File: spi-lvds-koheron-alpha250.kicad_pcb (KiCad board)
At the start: 2 copper layers, 55 x 50 mm, 17 parts

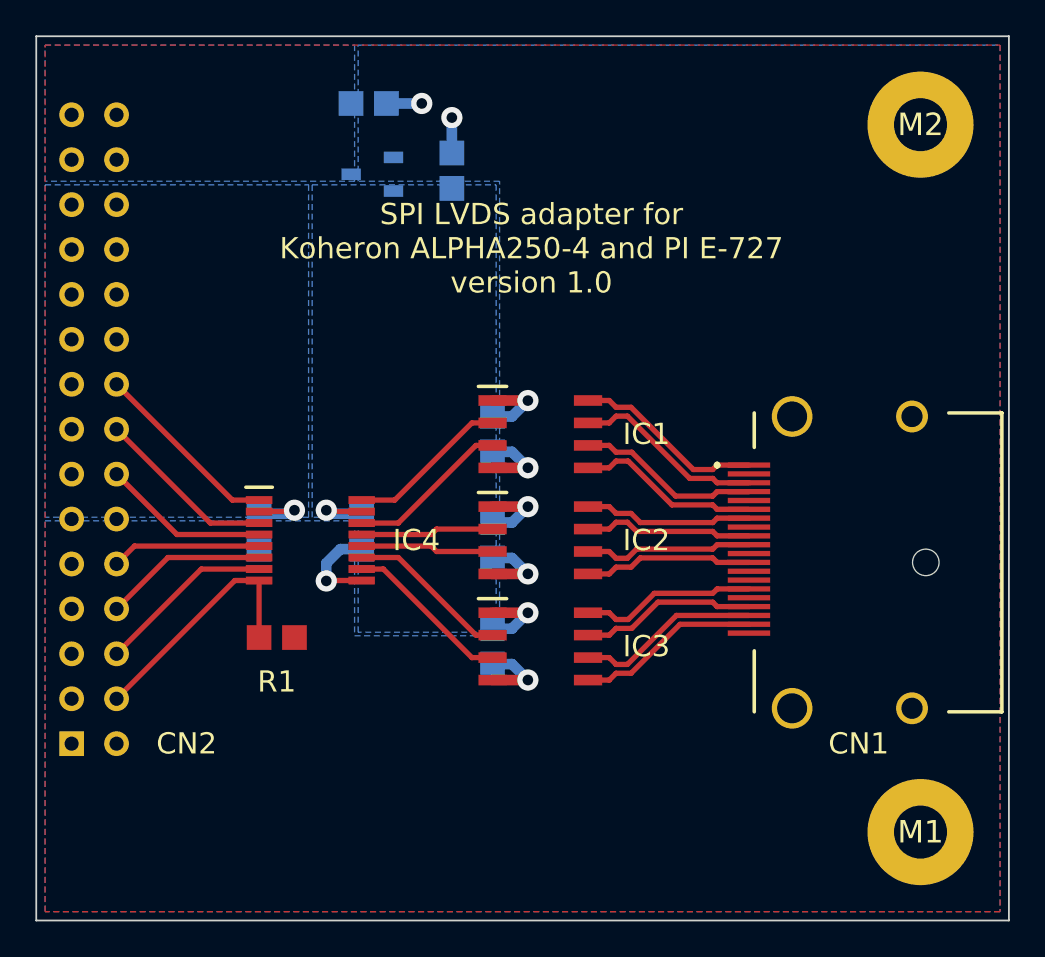
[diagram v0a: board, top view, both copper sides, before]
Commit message: improve PCB layout
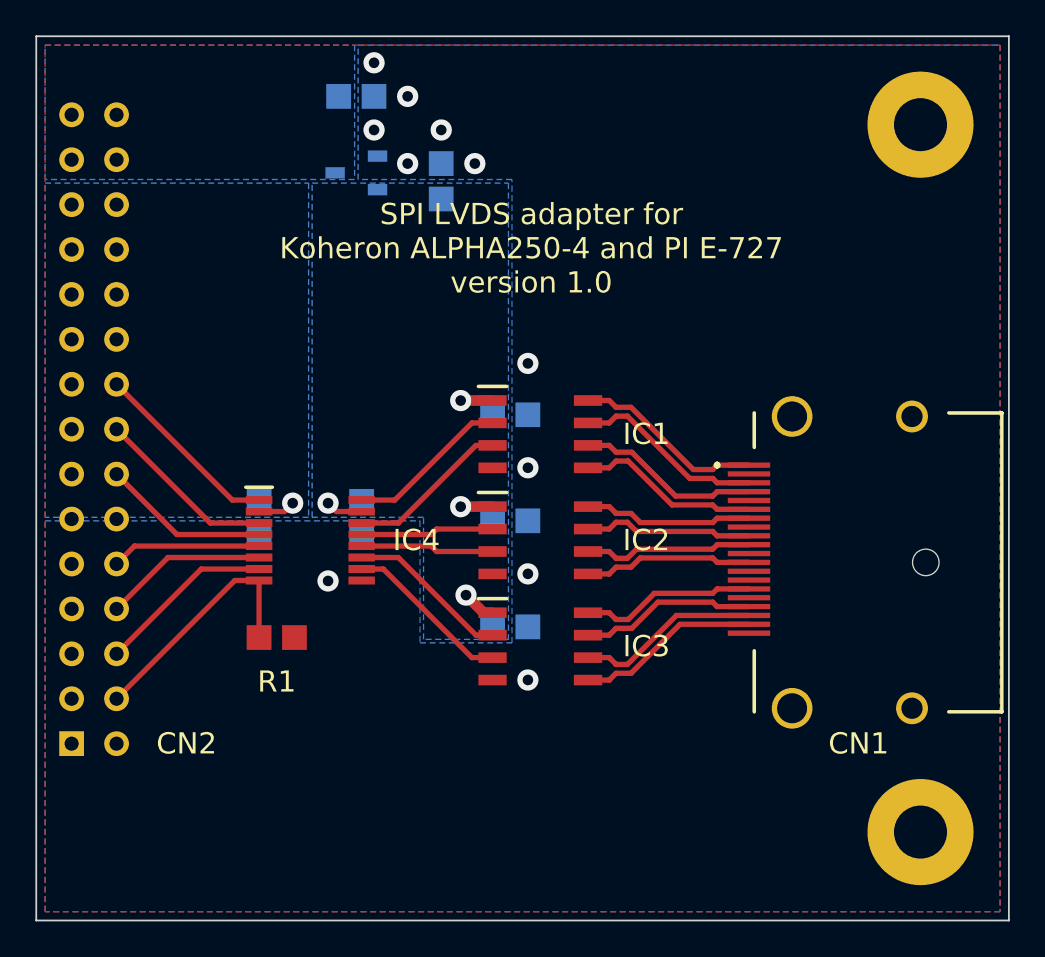
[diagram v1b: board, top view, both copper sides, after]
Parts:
- moved C1 1.49 mm to (106.8, 81.4), turned to 0 degrees
- moved C2 1.49 mm to (106.8, 87.4), turned to 0 degrees
- moved C3 1.49 mm to (106.8, 93.4), turned to 0 degrees
- moved IC5 0.90 mm to (98.1, 67.7)
- moved C7 0.85 mm to (102.9, 68.2)
- moved C6 0.81 mm to (98.1, 63.4)
- moved C4 0.70 mm to (92.6, 87.3)
- moved C5 0.70 mm to (98.4, 87.3)
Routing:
- net GND: track 23.3 -> 0.00 mm, vias 6 -> 11
- net 3V3: track 17.2 -> 7.61 mm
- net 1V8: track 4.11 -> 2.10 mm
